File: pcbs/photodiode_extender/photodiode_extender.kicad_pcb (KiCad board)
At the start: 2 copper layers, 15 x 20 mm, 44 parts, among them J1 CONN_01X01, J2 CONN_01X01, J3 CONN_01X01

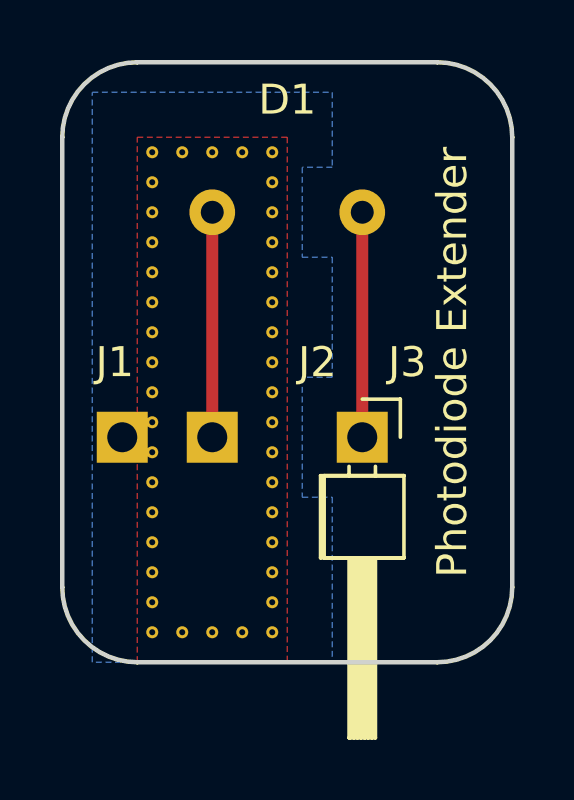
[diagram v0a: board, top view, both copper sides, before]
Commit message: Finished the photo extender, backplane and the analog board.
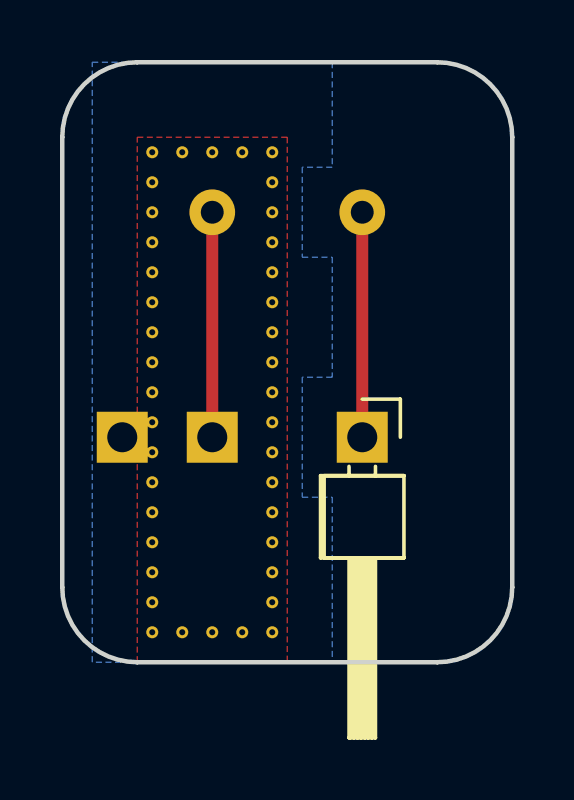
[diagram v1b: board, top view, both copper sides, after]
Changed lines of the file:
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@@
     (links 42)
     (no_connects 0)
-    (area 119.924999 79.924999 135.075001 100.075001)
+    (area 107.150001 71.8 173.214288 123.175)
     (thickness 1.6)
-    (drawings 15)
+    (drawings 16)
     (tracks 2)
     (zones 0)
@@
     (descr "Through hole angled pin header, 1x01, 2.54mm pitch, 6mm pin length, single row")
     (tags "Through hole angled pin header THT 1x01 2.54mm single row")
-    (fp_text reference J3 (at -2.5 -1.5 360) (layer F.SilkS)
-      (effects (font (size 1 1) (thickness 0.15)))
+    (fp_text reference J3 (at -2.5 0 360) (layer B.SilkS)
+      (effects (font (size 1 1) (thickness 0.15)) (justify mirror))
     )
     (fp_text value CONN_01X01 (at 4.315 2.27 270) (layer F.Fab)
@@
   (module Photodiodes:BPW34FA_w_Silks (layer F.Cu)
     (at 127.5 85)
-    (fp_text reference D1 (at 0 -3.75) (layer F.SilkS)
-      (effects (font (size 1 1) (thickness 0.15)))
+    (fp_text reference D1 (at 0 -3.75) (layer B.SilkS)
+      (effects (font (size 1 1) (thickness 0.15)) (justify mirror))
     )
     (fp_text value D_Photo (at 0 -3.81) (layer F.Fab)
@@
     (descr "Through hole angled pin header, 1x01, 2.54mm pitch, 6mm pin length, single row")
     (tags "Through hole angled pin header THT 1x01 2.54mm single row")
-    (fp_text reference J1 (at -2.5 0.25 360) (layer F.SilkS)
-      (effects (font (size 1 1) (thickness 0.15)))
+    (fp_text reference J1 (at -2.5 0.25 360) (layer B.SilkS)
+      (effects (font (size 1 1) (thickness 0.15)) (justify mirror))
     )
     (fp_text value CONN_01X01 (at 4.315 2.27 270) (layer F.Fab)
@@
     (descr "Through hole angled pin header, 1x01, 2.54mm pitch, 6mm pin length, single row")
     (tags "Through hole angled pin header THT 1x01 2.54mm single row")
-    (fp_text reference J2 (at -2.5 -3.5 360) (layer F.SilkS)
-      (effects (font (size 1 1) (thickness 0.15)))
+    (fp_text reference J2 (at -2.5 0 360) (layer B.SilkS)
+      (effects (font (size 1 1) (thickness 0.15)) (justify mirror))
     )
     (fp_text value CONN_01X01 (at 4.315 2.27 270) (layer F.Fab)
@@
     )
   )
+  (dimension 5 (width 0.3) (layer Dwgs.User)
+    (gr_text "5,0 mm" (at 128 110) (layer Dwgs.User)
+      (effects (font (size 1.5 1.5) (thickness 0.3)))
+    )
+    (feature1 (pts (xy 130 102) (xy 130 108.7)))
+    (feature2 (pts (xy 125 102) (xy 125 108.7)))
+    (crossbar (pts (xy 125 106) (xy 130 106)))
+    (arrow1a (pts (xy 130 106) (xy 128.873496 106.586421)))
+    (arrow1b (pts (xy 130 106) (xy 128.873496 105.413579)))
+    (arrow2a (pts (xy 125 106) (xy 126.126504 106.586421)))
+    (arrow2b (pts (xy 125 106) (xy 126.126504 105.413579)))
+  )
   (dimension 3 (width 0.3) (layer Dwgs.User)
     (gr_text "3,0 mm" (at 127 76.25) (layer Dwgs.User)
@@
     (arrow2b (pts (xy 122 79.75) (xy 123.126504 79.163579)))
   )
-  (gr_text "Photodiode Extender" (at 133 90 90) (layer F.SilkS)
-    (effects (font (size 1 1) (thickness 0.2)))
-  )
-  (gr_text "5.84 + 2.54 + 1.52 = 9.9\n9.9  - 7.5 = 2.4\n2.4 - 1.6 = 0.8  \nThis is the length the headers will stand out with." (at 114.5 108.5) (layer Dwgs.User)
+  (gr_text "Photodiode Extender" (at 133.25 90 90) (layer B.SilkS)
+    (effects (font (size 1 1) (thickness 0.2)) (justify mirror))
+  )
+  (gr_text "5.84 + 2.54 + 1.52 = 9.9\n9.9  - 7.5 = 2.4\n2.4 - 1.6 = 0.8  \nThis is the length the headers will stand out with." (at 115 118) (layer Dwgs.User)
     (effects (font (size 1.5 1.5) (thickness 0.3)) (justify left))
   )
@@
     (polygon
       (pts
-        (xy 121 81) (xy 129 81) (xy 129 83.5) (xy 128 83.5) (xy 128 86.5)
+        (xy 121 80) (xy 129 80) (xy 129 83.5) (xy 128 83.5) (xy 128 86.5)
         (xy 129 86.5) (xy 129 90.5) (xy 128 90.5) (xy 128 94.5) (xy 129 94.5)
         (xy 129 100) (xy 121 100)

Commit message: Added BOMs and gerber files.
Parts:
- added REF**: Stitching-Via-0.2-0.4, Vias:Stitchging-Via-0.2-0.4, F.Cu at (126.0, 99.0)
- added REF**: Stitching-Via-0.2-0.4, Vias:Stitchging-Via-0.2-0.4, F.Cu at (125.0, 99.0)
- added REF**: Stitching-Via-0.2-0.4, Vias:Stitchging-Via-0.2-0.4, F.Cu at (124.0, 99.0)
- moved REF** 4.00 mm to (124.0, 95.0)
- moved REF** 4.00 mm to (125.0, 95.0)
- moved REF** 4.00 mm to (126.0, 95.0)
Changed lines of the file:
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@@
 (kicad_pcb (version 4) (host pcbnew 4.0.6-e0-6349~52~ubuntu17.04.1)
   (general
-    (links 42)
+    (links 45)
     (no_connects 0)
     (area 107.150001 71.8 173.214288 123.175)
@@
     (tracks 2)
     (zones 0)
-    (modules 44)
+    (modules 47)
     (nets 4)
   )
@@
     (47 F.CrtYd user)
     (48 B.Fab user)
-    (49 F.Fab user)
+    (49 F.Fab user hide)
   )
   (setup
@@
     (pad_to_mask_clearance 0.2)
     (aux_axis_origin 0 0)
-    (visible_elements FFFFFF7F)
+    (visible_elements FFFFFF1F)
     (pcbplotparams
-      (layerselection 0x00030_80000001)
+      (layerselection 0x010f0_80000001)
       (usegerberextensions false)
       (excludeedgelayer true)
@@
       (outputformat 1)
       (mirror false)
-      (drillshape 1)
+      (drillshape 0)
       (scaleselection 1)
-      (outputdirectory ""))
+      (outputdirectory output/gerber/))
   )
   (net 0 "")
@@
   )
   (module Vias:Stitchging-Via-0.2-0.4 (layer F.Cu)
+    (at 126 99)
+    (fp_text reference REF** (at 0 1.27) (layer F.SilkS) hide
+      (effects (font (size 1 1) (thickness 0.15)))
+    )
+    (fp_text value Stitching-Via-0.2-0.4 (at 0 -1.27) (layer F.Fab) hide
+      (effects (font (size 1 1) (thickness 0.15)))
+    )
+    (pad ~ thru_hole circle (at 0 0) (size 0.4 0.4) (drill 0.2) (layers *.Cu)
+      (net 3 GNDA) (zone_connect 2))
+  )
+  (module Vias:Stitchging-Via-0.2-0.4 (layer F.Cu)
+    (at 125 99)
+    (fp_text reference REF** (at 0 1.27) (layer F.SilkS) hide
+      (effects (font (size 1 1) (thickness 0.15)))
+    )
+    (fp_text value Stitching-Via-0.2-0.4 (at 0 -1.27) (layer F.Fab) hide
+      (effects (font (size 1 1) (thickness 0.15)))
+    )
+    (pad ~ thru_hole circle (at 0 0) (size 0.4 0.4) (drill 0.2) (layers *.Cu)
+      (net 3 GNDA) (zone_connect 2))
+  )
+  (module Vias:Stitchging-Via-0.2-0.4 (layer F.Cu)
+    (at 124 99)
+    (fp_text reference REF** (at 0 1.27) (layer F.SilkS) hide
+      (effects (font (size 1 1) (thickness 0.15)))
+    )
+    (fp_text value Stitching-Via-0.2-0.4 (at 0 -1.27) (layer F.Fab) hide
+      (effects (font (size 1 1) (thickness 0.15)))
+    )
+    (pad ~ thru_hole circle (at 0 0) (size 0.4 0.4) (drill 0.2) (layers *.Cu)
+      (net 3 GNDA) (zone_connect 2))
+  )
+  (module Vias:Stitchging-Via-0.2-0.4 (layer F.Cu)
+    (at 127 96)
+    (fp_text reference REF** (at 0 1.27) (layer F.SilkS) hide
+      (effects (font (size 1 1) (thickness 0.15)))
+    )
+    (fp_text value Stitching-Via-0.2-0.4 (at 0 -1.27) (layer F.Fab) hide
+      (effects (font (size 1 1) (thickness 0.15)))
+    )
+    (pad ~ thru_hole circle (at 0 0) (size 0.4 0.4) (drill 0.2) (layers *.Cu)
+      (net 3 GNDA) (zone_connect 2))
+  )
+  (module Vias:Stitchging-Via-0.2-0.4 (layer F.Cu)
+    (at 127 97)
+    (fp_text reference REF** (at 0 1.27) (layer F.SilkS) hide
+      (effects (font (size 1 1) (thickness 0.15)))
+    )
+    (fp_text value Stitching-Via-0.2-0.4 (at 0 -1.27) (layer F.Fab) hide
+      (effects (font (size 1 1) (thickness 0.15)))
+    )
+    (pad ~ thru_hole circle (at 0 0) (size 0.4 0.4) (drill 0.2) (layers *.Cu)
+      (net 3 GNDA) (zone_connect 2))
+  )
+  (module Vias:Stitchging-Via-0.2-0.4 (layer F.Cu)
+    (at 127 98)
+    (fp_text reference REF** (at 0 1.27) (layer F.SilkS) hide
+      (effects (font (size 1 1) (thickness 0.15)))
+    )
+    (fp_text value Stitching-Via-0.2-0.4 (at 0 -1.27) (layer F.Fab) hide
+      (effects (font (size 1 1) (thickness 0.15)))
+    )
+    (pad ~ thru_hole circle (at 0 0) (size 0.4 0.4) (drill 0.2) (layers *.Cu)
+      (net 3 GNDA) (zone_connect 2))
+  )
+  (module Vias:Stitchging-Via-0.2-0.4 (layer F.Cu)
+    (at 127 99)
+    (fp_text reference REF** (at 0 1.27) (layer F.SilkS) hide
+      (effects (font (size 1 1) (thickness 0.15)))
+    )
+    (fp_text value Stitching-Via-0.2-0.4 (at 0 -1.27) (layer F.Fab) hide
+      (effects (font (size 1 1) (thickness 0.15)))
+    )
+    (pad ~ thru_hole circle (at 0 0) (size 0.4 0.4) (drill 0.2) (layers *.Cu)
+      (net 3 GNDA) (zone_connect 2))
+  )
+  (module Vias:Stitchging-Via-0.2-0.4 (layer F.Cu)
     (at 123 85)
     (fp_text reference REF** (at 0 1.27) (layer F.SilkS) hide
@@
   )
   (module Vias:Stitchging-Via-0.2-0.4 (layer F.Cu)
-    (at 127 96)
-    (fp_text reference REF** (at 0 1.27) (layer F.SilkS) hide
-      (effects (font (size 1 1) (thickness 0.15)))
-    )
-    (fp_text value Stitching-Via-0.2-0.4 (at 0 -1.27) (layer F.Fab) hide
-      (effects (font (size 1 1) (thickness 0.15)))
-    )
-    (pad ~ thru_hole circle (at 0 0) (size 0.4 0.4) (drill 0.2) (layers *.Cu)
-      (net 3 GNDA) (zone_connect 2))
-  )
-  (module Vias:Stitchging-Via-0.2-0.4 (layer F.Cu)
-    (at 127 97)
-    (fp_text reference REF** (at 0 1.27) (layer F.SilkS) hide
-      (effects (font (size 1 1) (thickness 0.15)))
-    )
-    (fp_text value Stitching-Via-0.2-0.4 (at 0 -1.27) (layer F.Fab) hide
-      (effects (font (size 1 1) (thickness 0.15)))
-    )
-    (pad ~ thru_hole circle (at 0 0) (size 0.4 0.4) (drill 0.2) (layers *.Cu)
-      (net 3 GNDA) (zone_connect 2))
-  )
-  (module Vias:Stitchging-Via-0.2-0.4 (layer F.Cu)
-    (at 127 98)
-    (fp_text reference REF** (at 0 1.27) (layer F.SilkS) hide
-      (effects (font (size 1 1) (thickness 0.15)))
-    )
-    (fp_text value Stitching-Via-0.2-0.4 (at 0 -1.27) (layer F.Fab) hide
-      (effects (font (size 1 1) (thickness 0.15)))
-    )
-    (pad ~ thru_hole circle (at 0 0) (size 0.4 0.4) (drill 0.2) (layers *.Cu)
-      (net 3 GNDA) (zone_connect 2))
-  )
-  (module Vias:Stitchging-Via-0.2-0.4 (layer F.Cu)
     (at 123 86)
     (fp_text reference REF** (at 0 1.27) (layer F.SilkS) hide
@@
   )
   (module Vias:Stitchging-Via-0.2-0.4 (layer F.Cu)
-    (at 124 99)
-    (fp_text reference REF** (at 0 1.27) (layer F.SilkS) hide
-      (effects (font (size 1 1) (thickness 0.15)))
-    )
-    (fp_text value Stitching-Via-0.2-0.4 (at 0 -1.27) (layer F.Fab) hide
-      (effects (font (size 1 1) (thickness 0.15)))
-    )
-    (pad ~ thru_hole circle (at 0 0) (size 0.4 0.4) (drill 0.2) (layers *.Cu)
-      (net 3 GNDA) (zone_connect 2))
-  )
-  (module Vias:Stitchging-Via-0.2-0.4 (layer F.Cu)
-    (at 125 99)
-    (fp_text reference REF** (at 0 1.27) (layer F.SilkS) hide
-      (effects (font (size 1 1) (thickness 0.15)))
-    )
-    (fp_text value Stitching-Via-0.2-0.4 (at 0 -1.27) (layer F.Fab) hide
-      (effects (font (size 1 1) (thickness 0.15)))
-    )
-    (pad ~ thru_hole circle (at 0 0) (size 0.4 0.4) (drill 0.2) (layers *.Cu)
-      (net 3 GNDA) (zone_connect 2))
-  )
-  (module Vias:Stitchging-Via-0.2-0.4 (layer F.Cu)
-    (at 126 99)
+    (at 124 95)
+    (fp_text reference REF** (at 0 1.27) (layer F.SilkS) hide
+      (effects (font (size 1 1) (thickness 0.15)))
+    )
+    (fp_text value Stitching-Via-0.2-0.4 (at 0 -1.27) (layer F.Fab) hide
+      (effects (font (size 1 1) (thickness 0.15)))
+    )
+    (pad ~ thru_hole circle (at 0 0) (size 0.4 0.4) (drill 0.2) (layers *.Cu)
+      (net 3 GNDA) (zone_connect 2))
+  )
+  (module Vias:Stitchging-Via-0.2-0.4 (layer F.Cu)
+    (at 125 95)
+    (fp_text reference REF** (at 0 1.27) (layer F.SilkS) hide
+      (effects (font (size 1 1) (thickness 0.15)))
+    )
+    (fp_text value Stitching-Via-0.2-0.4 (at 0 -1.27) (layer F.Fab) hide
+      (effects (font (size 1 1) (thickness 0.15)))
+    )
+    (pad ~ thru_hole circle (at 0 0) (size 0.4 0.4) (drill 0.2) (layers *.Cu)
+      (net 3 GNDA) (zone_connect 2))
+  )
+  (module Vias:Stitchging-Via-0.2-0.4 (layer F.Cu)
+    (at 126 95)
     (fp_text reference REF** (at 0 1.27) (layer F.SilkS) hide
       (effects (font (size 1 1) (thickness 0.15)))
@@
     )
   )
-  (module Vias:Stitchging-Via-0.2-0.4 (layer F.Cu)
-    (at 127 99)
-    (fp_text reference REF** (at 0 1.27) (layer F.SilkS) hide
-      (effects (font (size 1 1) (thickness 0.15)))
-    )
-    (fp_text value Stitching-Via-0.2-0.4 (at 0 -1.27) (layer F.Fab) hide
-      (effects (font (size 1 1) (thickness 0.15)))
-    )
-    (pad ~ thru_hole circle (at 0 0) (size 0.4 0.4) (drill 0.2) (layers *.Cu)
-      (net 3 GNDA) (zone_connect 2))
-  )
   (module Photodiodes:BPW34FA_w_Silks (layer F.Cu)
